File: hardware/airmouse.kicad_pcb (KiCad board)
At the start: 2 copper layers, 18.5 x 36.6 mm, 25 parts, among them J1 USB_C_Receptacle_USB2.0_16P, J2 Conn_01x07_Pin, U1 XC6206PxxxMR, U2 MPU-9250, U3 STM32F103CBTx, Y1 8MHz

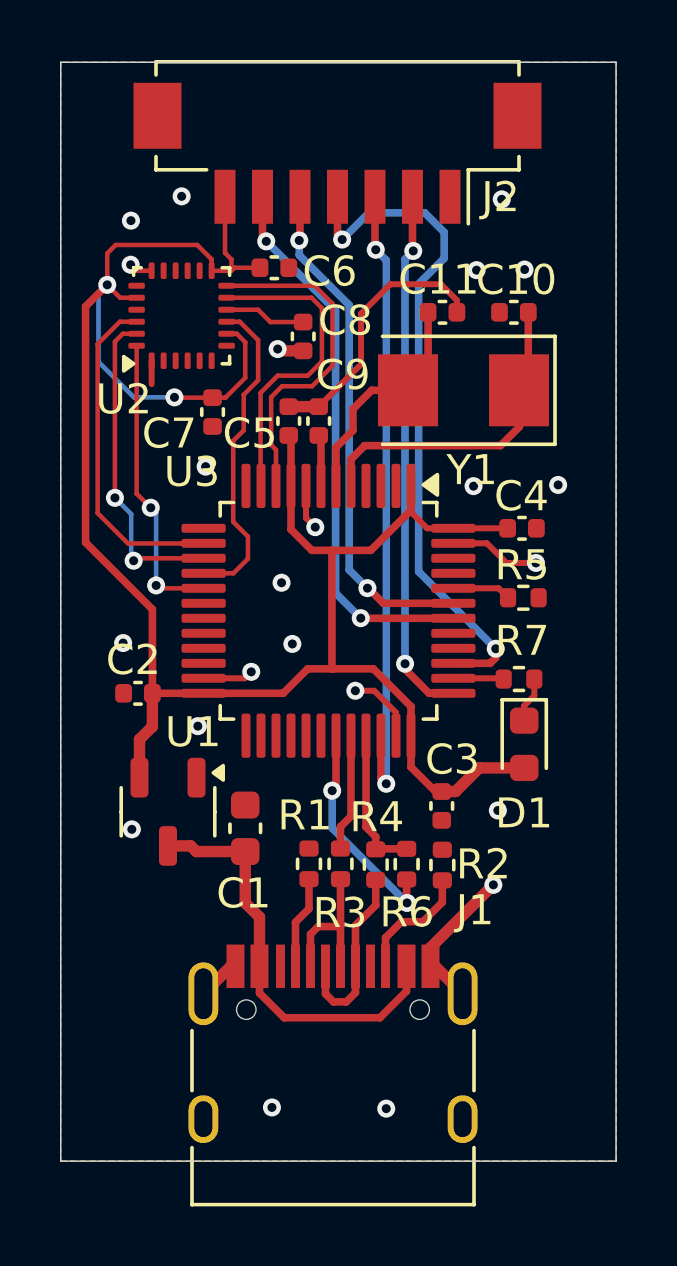
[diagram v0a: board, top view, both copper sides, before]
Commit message: 修改MPU-9250为ICM-20948
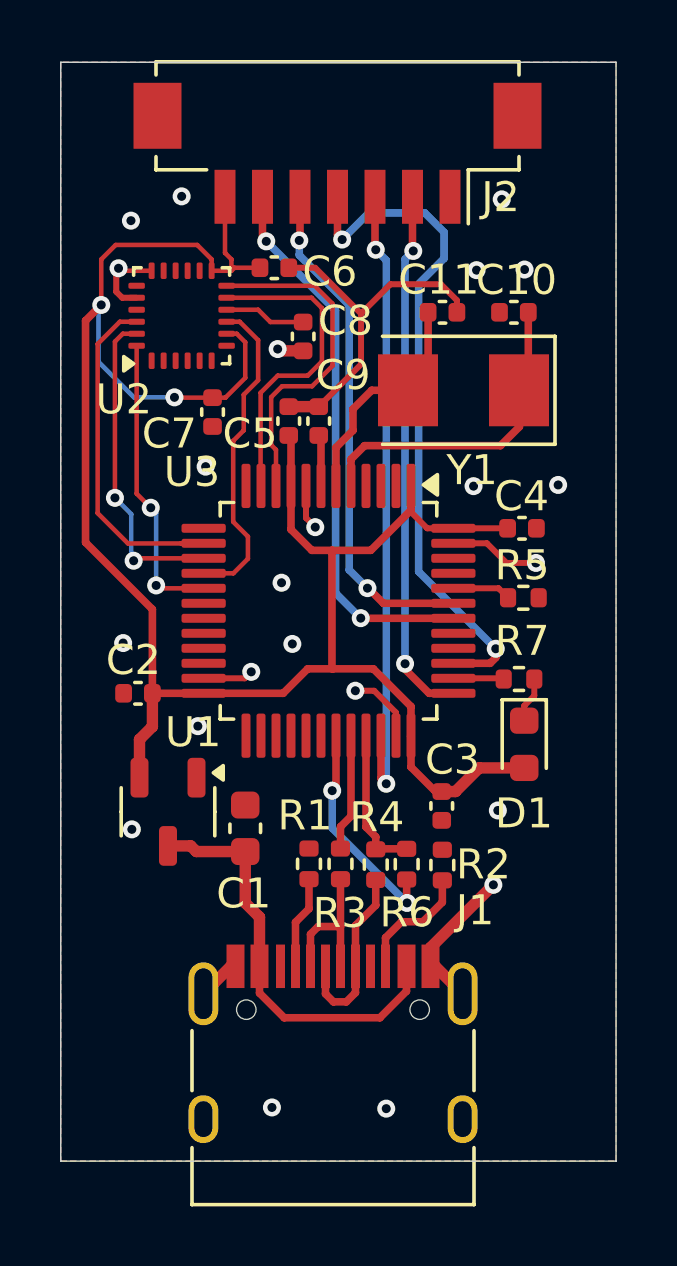
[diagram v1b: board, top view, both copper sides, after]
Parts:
- U2: value MPU-9250 -> ICM-20948
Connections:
- net /MPU_9250_FSYNC renamed /ICM_20948_FSYNC
- net /MPU_9250_INT renamed /ICM_20948_INT
- U2 pad 1: GND -> unconnected-(U2-NC-Pad1)
- U2 pad 14: (no net) -> unconnected-(U2-NC-Pad14)
- U2 pad 15: (no net) -> unconnected-(U2-NC-Pad15)
- U2 pad 16: (no net) -> unconnected-(U2-NC-Pad16)
- U2 pad 17: (no net) -> unconnected-(U2-NC-Pad17)
- U2 pad 19: (no net) -> unconnected-(U2-RESV-Pad19)
- U2 pad 2: (no net) -> unconnected-(U2-NC-Pad2)
- U2 pad 20: +3V3 -> GND
- U2 pad 3: (no net) -> unconnected-(U2-NC-Pad3)
- U2 pad 4: (no net) -> unconnected-(U2-NC-Pad4)
- U2 pad 5: (no net) -> unconnected-(U2-NC-Pad5)
- U2 pad 6: (no net) -> unconnected-(U2-NC-Pad6)
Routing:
- net GND: track 26.5 -> 30.6 mm
- net +3V3: track 71.7 -> 69.8 mm
